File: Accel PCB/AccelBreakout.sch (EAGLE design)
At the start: 8 parts

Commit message: Fixed silk screen and added accelerometer directions
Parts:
- removed SV1: (no value), con-lstb:MA06-1
- added U$1: DIP1X6MALE, ScottSilver:DIP1X6MALE
- added U$2: ACCELDIR, ScottSilver:ACCELDIR
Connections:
- net GND: now also U$1.6; no longer SV1.6
- net INT1: now also U$1.4; no longer SV1.4
- net INT2: now also U$1.5; no longer SV1.5
- net SCL: now also U$1.3; no longer SV1.3
- net SDA: now also U$1.2; no longer SV1.2
- net VCC: now also U$1.1; no longer SV1.1
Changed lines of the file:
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@@
 <part name="SUPPLY1" library="SparkFun-Aesthetics" deviceset="VCC" device=""/>
 <part name="GND1" library="SparkFun-Aesthetics" deviceset="GND" device=""/>
-<part name="SV1" library="con-lstb" deviceset="MA06-1" device=""/>
+<part name="U$1" library="ScottSilver" deviceset="DIP1X6MALE" device=""/>
+<part name="U$2" library="ScottSilver" deviceset="ACCELDIR" device=""/>
 </parts>
 <sheets>
@@
 <instance part="SUPPLY1" gate="G$1" x="0" y="38.1"/>
 <instance part="GND1" gate="1" x="0" y="22.86"/>
-<instance part="SV1" gate="1" x="-10.16" y="30.48" rot="MR180"/>
+<instance part="U$1" gate="G$1" x="-5.08" y="33.02" rot="MR180"/>
+<instance part="U$2" gate="G$1" x="81.28" y="20.32"/>
 </instances>
 <busses>
@@
 <segment>
 <pinref part="SUPPLY1" gate="G$1" pin="VCC"/>
-<wire x1="-2.54" y1="38.1" x2="0" y2="38.1" width="0.1524" layer="91"/>
-<pinref part="SV1" gate="1" pin="1"/>
+<wire x1="-5.08" y1="38.1" x2="0" y2="38.1" width="0.1524" layer="91"/>
+<pinref part="U$1" gate="G$1" pin="1"/>
 </segment>
 </net>
@@
 <segment>
 <pinref part="GND1" gate="1" pin="GND"/>
-<wire x1="0" y1="25.4" x2="-2.54" y2="25.4" width="0.1524" layer="91"/>
-<pinref part="SV1" gate="1" pin="6"/>
+<wire x1="0" y1="25.4" x2="-5.08" y2="25.4" width="0.1524" layer="91"/>
+<pinref part="U$1" gate="G$1" pin="6"/>
 </segment>
 </net>
@@
 </segment>
 <segment>
-<pinref part="SV1" gate="1" pin="2"/>
-<wire x1="-2.54" y1="35.56" x2="0" y2="35.56" width="0.1524" layer="91"/>
+<wire x1="-5.08" y1="35.56" x2="0" y2="35.56" width="0.1524" layer="91"/>
 <label x="0" y="35.56" size="1.016" layer="95" xref="yes"/>
+<pinref part="U$1" gate="G$1" pin="2"/>
 </segment>
 </net>
@@
 </segment>
 <segment>
-<pinref part="SV1" gate="1" pin="3"/>
-<wire x1="-2.54" y1="33.02" x2="0" y2="33.02" width="0.1524" layer="91"/>
+<wire x1="-5.08" y1="33.02" x2="0" y2="33.02" width="0.1524" layer="91"/>
 <label x="0" y="33.02" size="1.016" layer="95" xref="yes"/>
+<pinref part="U$1" gate="G$1" pin="3"/>
 </segment>
 </net>
@@
 </segment>
 <segment>
-<pinref part="SV1" gate="1" pin="4"/>
-<wire x1="-2.54" y1="30.48" x2="0" y2="30.48" width="0.1524" layer="91"/>
+<wire x1="-5.08" y1="30.48" x2="0" y2="30.48" width="0.1524" layer="91"/>
 <label x="0" y="30.48" size="1.016" layer="95" xref="yes"/>
+<pinref part="U$1" gate="G$1" pin="4"/>
 </segment>
 </net>
@@
 </segment>
 <segment>
-<pinref part="SV1" gate="1" pin="5"/>
-<wire x1="-2.54" y1="27.94" x2="0" y2="27.94" width="0.1524" layer="91"/>
+<wire x1="-5.08" y1="27.94" x2="0" y2="27.94" width="0.1524" layer="91"/>
 <label x="0" y="27.94" size="1.016" layer="95" xref="yes"/>
+<pinref part="U$1" gate="G$1" pin="5"/>
 </segment>
 </net>

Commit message: Fixed text and arrow orientaiton for accel PCB
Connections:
- net GND: now also U$1.1; no longer U$1.6
- net INT1: now also U$1.3; no longer U$1.4
- net INT2: now also U$1.2; no longer U$1.5
- net SCL: now also U$1.4; no longer U$1.3
- net SDA: now also U$1.5; no longer U$1.2
- net VCC: now also U$1.6; no longer U$1.1
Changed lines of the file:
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@@
 <instance part="SUPPLY1" gate="G$1" x="0" y="38.1"/>
 <instance part="GND1" gate="1" x="0" y="22.86"/>
-<instance part="U$1" gate="G$1" x="-5.08" y="33.02" rot="MR180"/>
+<instance part="U$1" gate="G$1" x="-10.16" y="30.48" rot="MR0"/>
 <instance part="U$2" gate="G$1" x="81.28" y="20.32"/>
 </instances>
@@
 <segment>
 <pinref part="SUPPLY1" gate="G$1" pin="VCC"/>
-<wire x1="-5.08" y1="38.1" x2="0" y2="38.1" width="0.1524" layer="91"/>
-<pinref part="U$1" gate="G$1" pin="1"/>
+<wire x1="-10.16" y1="38.1" x2="0" y2="38.1" width="0.1524" layer="91"/>
+<pinref part="U$1" gate="G$1" pin="6"/>
 </segment>
 </net>
@@
 <segment>
 <pinref part="GND1" gate="1" pin="GND"/>
-<wire x1="0" y1="25.4" x2="-5.08" y2="25.4" width="0.1524" layer="91"/>
-<pinref part="U$1" gate="G$1" pin="6"/>
+<wire x1="0" y1="25.4" x2="-10.16" y2="25.4" width="0.1524" layer="91"/>
+<pinref part="U$1" gate="G$1" pin="1"/>
 </segment>
 </net>
@@
 </segment>
 <segment>
-<wire x1="-5.08" y1="35.56" x2="0" y2="35.56" width="0.1524" layer="91"/>
 <label x="0" y="35.56" size="1.016" layer="95" xref="yes"/>
-<pinref part="U$1" gate="G$1" pin="2"/>
+<wire x1="-10.16" y1="35.56" x2="0" y2="35.56" width="0.1524" layer="91"/>
+<pinref part="U$1" gate="G$1" pin="5"/>
 </segment>
 </net>
@@
 </segment>
 <segment>
-<wire x1="-5.08" y1="33.02" x2="0" y2="33.02" width="0.1524" layer="91"/>
 <label x="0" y="33.02" size="1.016" layer="95" xref="yes"/>
-<pinref part="U$1" gate="G$1" pin="3"/>
+<wire x1="-10.16" y1="33.02" x2="0" y2="33.02" width="0.1524" layer="91"/>
+<pinref part="U$1" gate="G$1" pin="4"/>
 </segment>
 </net>
@@
 </segment>
 <segment>
-<wire x1="-5.08" y1="30.48" x2="0" y2="30.48" width="0.1524" layer="91"/>
 <label x="0" y="30.48" size="1.016" layer="95" xref="yes"/>
-<pinref part="U$1" gate="G$1" pin="4"/>
+<wire x1="-10.16" y1="30.48" x2="0" y2="30.48" width="0.1524" layer="91"/>
+<pinref part="U$1" gate="G$1" pin="3"/>
 </segment>
 </net>
@@
 </segment>
 <segment>
-<wire x1="-5.08" y1="27.94" x2="0" y2="27.94" width="0.1524" layer="91"/>
 <label x="0" y="27.94" size="1.016" layer="95" xref="yes"/>
-<pinref part="U$1" gate="G$1" pin="5"/>
+<wire x1="-10.16" y1="27.94" x2="0" y2="27.94" width="0.1524" layer="91"/>
+<pinref part="U$1" gate="G$1" pin="2"/>
 </segment>
 </net>

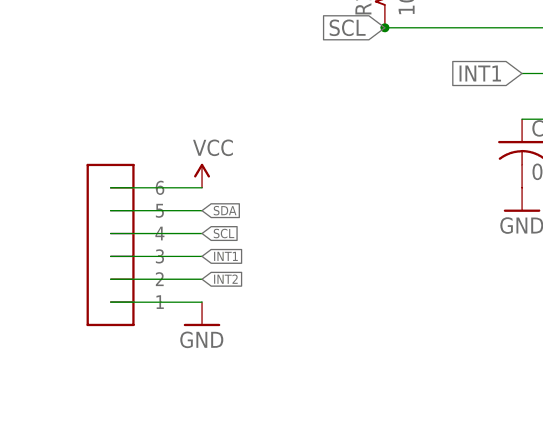
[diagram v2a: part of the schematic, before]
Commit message: Split 1x6 header into 2 1x3 headers 300 mils apart to fit over center bridge on breadboard
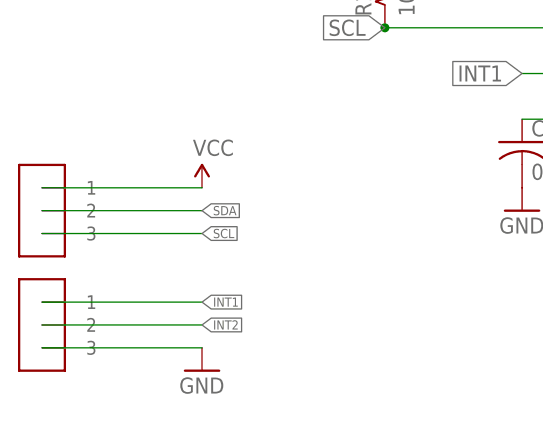
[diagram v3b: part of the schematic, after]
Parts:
- removed U$1: DIP1X6MALE, ScottSilver:DIP1X6MALE
- added U$3, U$4: DIP1X3MALE, OldScottSilver:DIP1X3MALE
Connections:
- net GND: now also U$4.3; no longer U$1.1
- net INT1: now also U$4.1; no longer U$1.3
- net INT2: now also U$4.2; no longer U$1.2
- net SCL: now also U$3.3; no longer U$1.4
- net SDA: now also U$3.2; no longer U$1.5
- net VCC: now also U$3.1; no longer U$1.6
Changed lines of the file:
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@@
 <?xml version="1.0" encoding="utf-8"?>
 <!DOCTYPE eagle SYSTEM "eagle.dtd">
-<eagle version="6.5.0">
+<eagle version="7.0.0">
 <drawing>
 <settings>
@@
 <part name="SUPPLY1" library="SparkFun-Aesthetics" deviceset="VCC" device=""/>
 <part name="GND1" library="SparkFun-Aesthetics" deviceset="GND" device=""/>
-<part name="U$1" library="ScottSilver" deviceset="DIP1X6MALE" device=""/>
 <part name="U$2" library="ScottSilver" deviceset="ACCELDIR" device=""/>
+<part name="U$3" library="OldScottSilver" deviceset="DIP1X3MALE" device=""/>
+<part name="U$4" library="OldScottSilver" deviceset="DIP1X3MALE" device=""/>
 </parts>
 <sheets>
@@
 <instance part="R2" gate="G$1" x="83.82" y="66.04" rot="R90"/>
 <instance part="SUPPLY1" gate="G$1" x="0" y="38.1"/>
-<instance part="GND1" gate="1" x="0" y="22.86"/>
-<instance part="U$1" gate="G$1" x="-10.16" y="30.48" rot="MR0"/>
+<instance part="GND1" gate="1" x="0" y="17.78"/>
 <instance part="U$2" gate="G$1" x="81.28" y="20.32"/>
+<instance part="U$3" gate="G$1" x="-17.78" y="35.56"/>
+<instance part="U$4" gate="G$1" x="-17.78" y="22.86"/>
 </instances>
 <busses>
@@
 <segment>
 <pinref part="SUPPLY1" gate="G$1" pin="VCC"/>
-<wire x1="-10.16" y1="38.1" x2="0" y2="38.1" width="0.1524" layer="91"/>
-<pinref part="U$1" gate="G$1" pin="6"/>
+<wire x1="-17.78" y1="38.1" x2="0" y2="38.1" width="0.1524" layer="91"/>
+<pinref part="U$3" gate="G$1" pin="1"/>
 </segment>
 </net>
@@
 <segment>
 <pinref part="GND1" gate="1" pin="GND"/>
-<wire x1="0" y1="25.4" x2="-10.16" y2="25.4" width="0.1524" layer="91"/>
-<pinref part="U$1" gate="G$1" pin="1"/>
+<wire x1="0" y1="20.32" x2="-17.78" y2="20.32" width="0.1524" layer="91"/>
+<pinref part="U$4" gate="G$1" pin="3"/>
 </segment>
 </net>
@@
 <segment>
 <label x="0" y="35.56" size="1.016" layer="95" xref="yes"/>
-<wire x1="-10.16" y1="35.56" x2="0" y2="35.56" width="0.1524" layer="91"/>
-<pinref part="U$1" gate="G$1" pin="5"/>
+<wire x1="-17.78" y1="35.56" x2="0" y2="35.56" width="0.1524" layer="91"/>
+<pinref part="U$3" gate="G$1" pin="2"/>
 </segment>
 </net>
@@
 <segment>
 <label x="0" y="33.02" size="1.016" layer="95" xref="yes"/>
-<wire x1="-10.16" y1="33.02" x2="0" y2="33.02" width="0.1524" layer="91"/>
-<pinref part="U$1" gate="G$1" pin="4"/>
+<wire x1="-17.78" y1="33.02" x2="0" y2="33.02" width="0.1524" layer="91"/>
+<pinref part="U$3" gate="G$1" pin="3"/>
 </segment>
 </net>
@@
 </segment>
 <segment>
-<label x="0" y="30.48" size="1.016" layer="95" xref="yes"/>
-<wire x1="-10.16" y1="30.48" x2="0" y2="30.48" width="0.1524" layer="91"/>
-<pinref part="U$1" gate="G$1" pin="3"/>
+<label x="0" y="25.4" size="1.016" layer="95" xref="yes"/>
+<wire x1="-17.78" y1="25.4" x2="0" y2="25.4" width="0.1524" layer="91"/>
+<pinref part="U$4" gate="G$1" pin="1"/>
 </segment>
 </net>
@@
 </segment>
 <segment>
-<label x="0" y="27.94" size="1.016" layer="95" xref="yes"/>
-<wire x1="-10.16" y1="27.94" x2="0" y2="27.94" width="0.1524" layer="91"/>
-<pinref part="U$1" gate="G$1" pin="2"/>
-</segment>
-</net>
+<label x="0" y="22.86" size="1.016" layer="95" xref="yes"/>
+<wire x1="-17.78" y1="22.86" x2="0" y2="22.86" width="0.1524" layer="91"/>
+<pinref part="U$4" gate="G$1" pin="2"/>
+</segment>
+</net>
